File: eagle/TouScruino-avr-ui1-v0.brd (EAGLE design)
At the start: 53.3 x 59.7 mm, 48 parts, among them J1 AVR_ISP, Q1 8MHz, Q2 MMBT2222, Q3 8MHz, U1 ATMEGA1284P, U3 ARDUINO_SHIELD, U4 MCP73831, U5 MIC5209-3.3YS, X1 USB

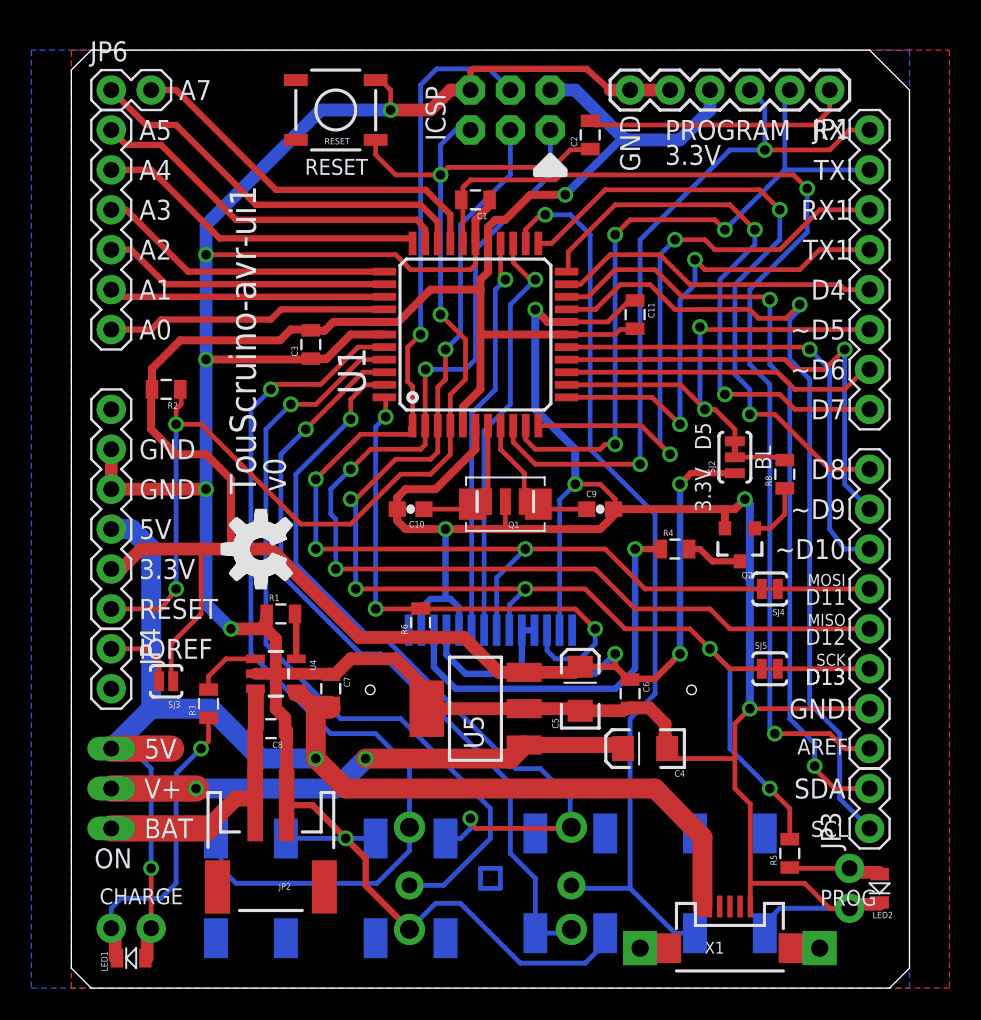
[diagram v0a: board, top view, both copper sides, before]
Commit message: 
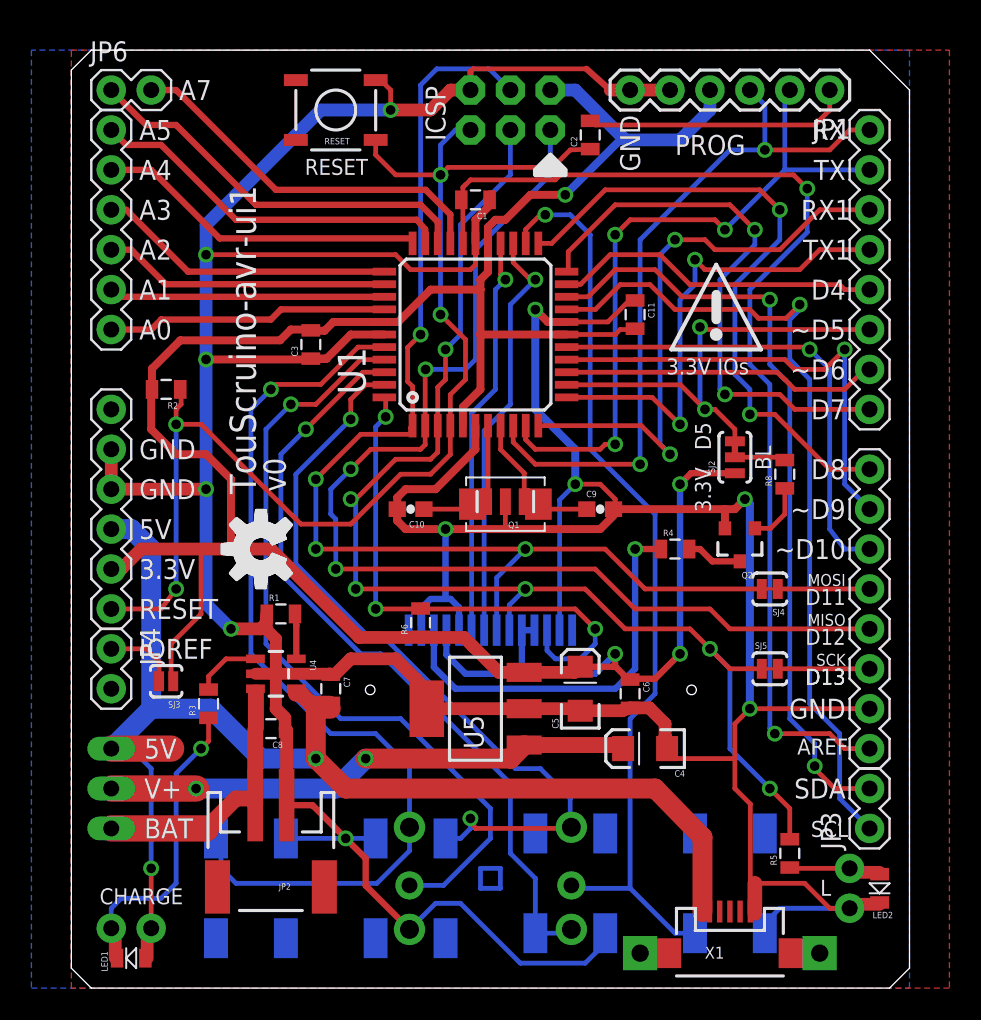
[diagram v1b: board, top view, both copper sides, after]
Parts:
- added U$6: 3.3V_IO, wibauxl:3.3V_IO
- JP1: value M06 -> M06TH
- moved X1 0.32 mm to (41.9, 2.22)
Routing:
- net GND: track 330.0 -> 330.7 mm
- net VUSB: track 84.6 -> 85.3 mm
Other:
- board text added: "L"
- board text removed: "ON"
- board text removed: "PROGRAM 3.3V"
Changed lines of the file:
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@@
 <setting verticaltext="up"/>
 </settings>
-<grid distance="12.5" unitdist="mil" unit="mm" style="lines" multiple="8" display="yes" altdistance="3.125" altunitdist="mil" altunit="mil"/>
+<grid distance="12.5" unitdist="mil" unit="mil" style="lines" multiple="8" display="yes" altdistance="3.125" altunitdist="mil" altunit="mil"/>
 <layers>
 <layer number="1" name="Top" color="4" fill="1" visible="yes" active="yes"/>
@@
 <layer number="27" name="tValues" color="7" fill="1" visible="no" active="yes"/>
 <layer number="28" name="bValues" color="7" fill="1" visible="no" active="yes"/>
-<layer number="29" name="tStop" color="7" fill="3" visible="no" active="yes"/>
+<layer number="29" name="tStop" color="7" fill="3" visible="yes" active="yes"/>
 <layer number="30" name="bStop" color="7" fill="6" visible="no" active="yes"/>
 <layer number="31" name="tCream" color="7" fill="4" visible="no" active="yes"/>
@@
 <layer number="220" name="220bmp" color="21" fill="1" visible="no" active="no"/>
 <layer number="221" name="221bmp" color="22" fill="1" visible="no" active="no"/>
+<layer number="222" name="222bmp" color="23" fill="1" visible="no" active="no"/>
 <layer number="223" name="223bmp" color="24" fill="1" visible="no" active="no"/>
 <layer number="224" name="224bmp" color="25" fill="1" visible="no" active="no"/>
@@
 <text x="44.529375" y="32.972375" size="1.016" layer="21" font="vector" ratio="15" distance="30" rot="R90">BL</text>
 <text x="39.6875" y="33.147" size="1.016" layer="21" font="vector" ratio="15" distance="30" rot="R270">3.3V</text>
-<text x="37.7825" y="52.3875" size="1.27" layer="21" font="vector" ratio="15" distance="25">PROGRAM
-3.3V</text>
+<text x="38.4175" y="53.0225" size="1.27" layer="21" font="vector" ratio="15" distance="25">PROG</text>
 <polygon width="0.3048" layer="21">
 <vertex x="30.48" y="53.0225"/>
@@
 <vertex x="31.4325" y="52.07"/>
 </polygon>
-<text x="1.4605" y="7.62" size="1.27" layer="21" font="vector" ratio="15">ON</text>
-<text x="47.6568" y="5.2387" size="1.016" layer="21" font="vector" ratio="15">PROG</text>
+<text x="47.6568" y="5.8737" size="1.016" layer="21" font="vector" ratio="15">L</text>
 </plain>
 <attributes>
@@
 <element name="JP2" library="SparkFun" package="JST-2-SMD" value="BAT" x="12.7" y="7.9375" rot="R180"/>
 <element name="C8" library="SparkFun" package="0805" value="4.7uF" x="12.7" y="16.51" rot="R180"/>
-<element name="X1" library="wibauxl" package="USB-MICROB" value="USB" x="41.91" y="2.54"/>
+<element name="X1" library="wibauxl" package="USB-MICROB" value="USB" x="41.91" y="2.2225"/>
 <element name="U$3" library="SparkFun" package="OSHW-LOGO-M" value="OSHW-LOGOM" x="12.065" y="27.94" rot="R90"/>
 <element name="JP5" library="wibauxl" package="1X3_LONGPAD" value="SWITCH" x="2.54" y="10.16" rot="MR270"/>
-<element name="JP1" library="wibauxl" package="1X06" value="M06" x="48.26" y="57.15" rot="R180"/>
+<element name="JP1" library="wibauxl" package="1X06" value="M06TH" x="48.26" y="57.15" rot="R180"/>
 <element name="J1" library="SparkFun" package="2X3" value="AVR_ISP" x="30.48" y="54.61" rot="MR0"/>
 <element name="JP3" library="wibauxl" package="1X02" value="I2C" x="50.8" y="10.16" rot="R90"/>
@@
 <element name="SJ4" library="SparkFun" package="SJ_2S-TRACE" value="" x="44.45" y="25.4" rot="R180"/>
 <element name="SJ5" library="SparkFun" package="SJ_2S-TRACE" value="" x="44.45" y="20.32"/>
+<element name="U$6" library="wibauxl" package="3.3V_IO" value="3.3V_IO" x="41.036875" y="42.2275"/>
 </elements>
 <signals>
@@
 <wire x1="35.56" y1="57.15" x2="34.29" y2="57.15" width="0.8128" layer="1"/>
 <wire x1="34.29" y1="57.15" x2="32.781875" y2="58.499375" width="0.4064" layer="1"/>
-<wire x1="32.781875" y1="58.499375" x2="25.55875" y2="58.499375" width="0.4064" layer="1"/>
-<wire x1="25.55875" y1="58.499375" x2="25.4" y2="58.340625" width="0.4064" layer="1"/>
+<wire x1="32.781875" y1="58.499375" x2="25.55875" y2="58.499375" width="0.3048" layer="1"/>
+<wire x1="25.55875" y1="58.499375" x2="25.4" y2="58.340625" width="0.3048" layer="1"/>
 <wire x1="25.4" y1="58.340625" x2="25.4" y2="57.4675" width="0.4064" layer="1"/>
 <wire x1="25.4" y1="57.4675" x2="25.4" y2="57.15" width="0.8128" layer="1"/>
@@
 <wire x1="42.2275" y1="16.8275" x2="42.2275" y2="14.605" width="0.3048" layer="1"/>
 <wire x1="42.2275" y1="16.8275" x2="43.18" y2="17.78" width="0.3048" layer="1"/>
-<wire x1="43.21" y1="5.19" x2="43.21" y2="6.6675" width="0.3048" layer="1"/>
+<wire x1="43.21" y1="4.8725" x2="43.4975" y2="4.7625" width="0.3048" layer="1"/>
+<wire x1="43.4975" y1="4.7625" x2="43.4975" y2="6.6675" width="0.9398" layer="1"/>
+<wire x1="43.4975" y1="6.6675" x2="43.21" y2="6.6675" width="0.3048" layer="1"/>
 <wire x1="43.21" y1="6.6675" x2="43.21" y2="11.7175" width="0.3048" layer="1"/>
 <wire x1="43.21" y1="11.7175" x2="42.2275" y2="12.7" width="0.3048" layer="1"/>
@@
 <wire x1="49.53" y1="5.08" x2="48.26" y2="5.08" width="0.3048" layer="1"/>
 <wire x1="48.26" y1="5.08" x2="46.6725" y2="6.6675" width="0.3048" layer="1"/>
-<wire x1="46.6725" y1="6.6675" x2="43.21" y2="6.6675" width="0.3048" layer="1"/>
+<wire x1="46.6725" y1="6.6675" x2="43.4975" y2="6.6675" width="0.3048" layer="1"/>
 <wire x1="44.1325" y1="4.1275" x2="45.085" y2="5.08" width="0.3048" layer="16"/>
 <wire x1="45.085" y1="5.08" x2="49.53" y2="5.08" width="0.3048" layer="16"/>
@@
 <wire x1="2.54" y1="15.24" x2="6.35" y2="15.24" width="1.6764" layer="1"/>
 <wire x1="5.08" y1="17.78" x2="2.54" y2="15.24" width="1.27" layer="16"/>
-<wire x1="40.3225" y1="5.19" x2="40.16375" y2="5.159375" width="0.4064" layer="1"/>
-<wire x1="40.16375" y1="5.159375" x2="40.16375" y2="9.604375" width="1.27" layer="1"/>
+<wire x1="40.3225" y1="5.19" x2="40.16375" y2="4.841875" width="0.4064" layer="1"/>
+<wire x1="40.16375" y1="4.841875" x2="40.16375" y2="9.604375" width="1.27" layer="1"/>
 <wire x1="40.16375" y1="9.604375" x2="37.1475" y2="12.7" width="1.27" layer="1"/>
-<wire x1="40.3225" y1="5.19" x2="40.61" y2="5.19" width="0.127" layer="1"/>
+<wire x1="40.3225" y1="5.19" x2="40.61" y2="4.8725" width="0.127" layer="1"/>
 </signal>
 <signal name="N$13">
@@
 </board>
 </drawing>
-<compatibility>
-<note version="6.3" minversion="6.2.2" severity="warning">
-Since Version 6.2.2 text objects can contain more than one line,
-which will not be processed correctly with this version.
-</note>
-</compatibility>
 </eagle>

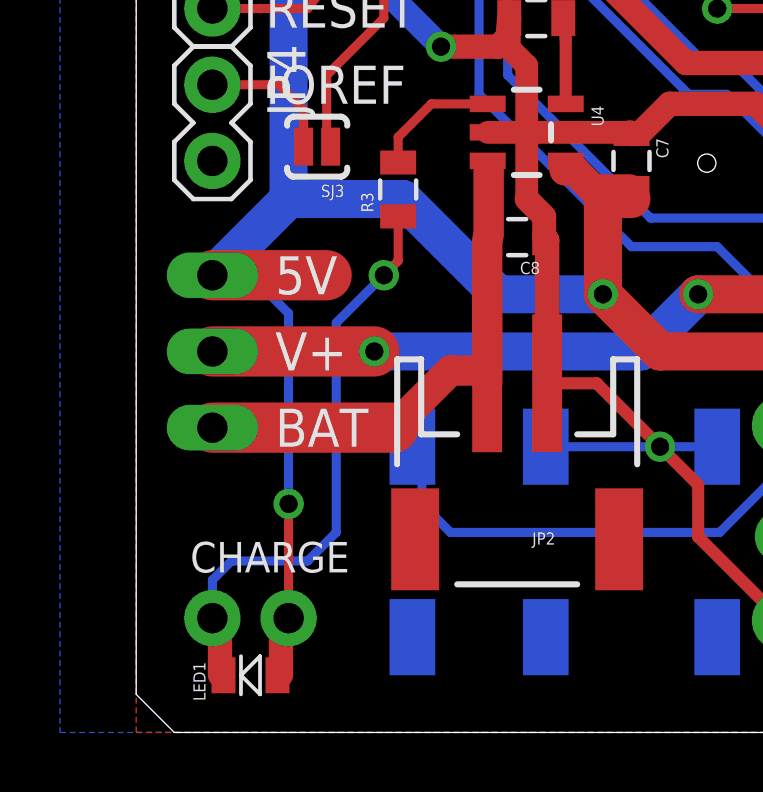
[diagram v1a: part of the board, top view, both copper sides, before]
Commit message: 
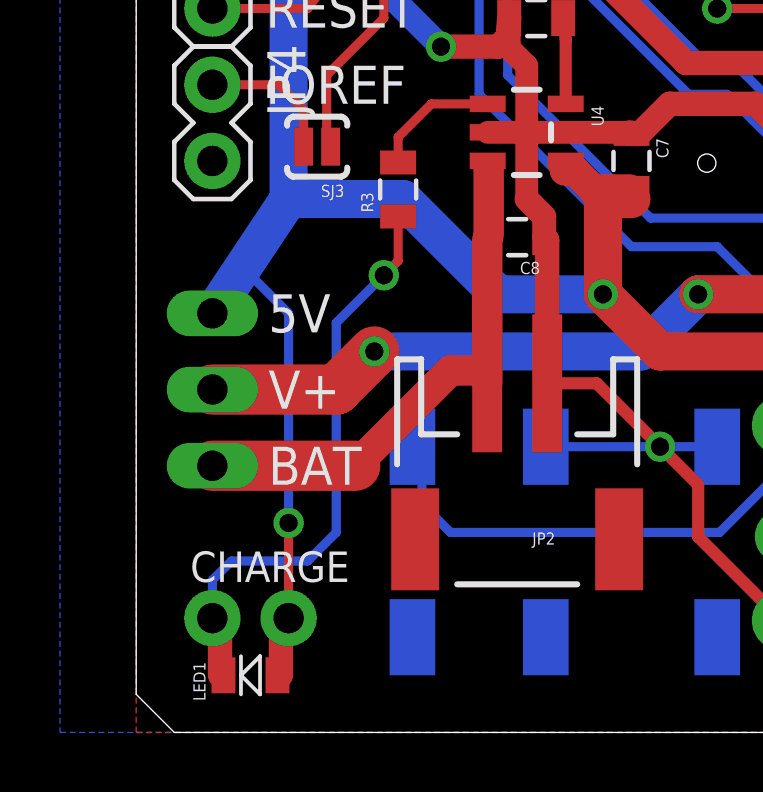
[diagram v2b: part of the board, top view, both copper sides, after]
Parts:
- moved JP5 1.27 mm to (2.54, 8.89)
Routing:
- net VUSB: track 85.3 -> 83.0 mm
- net VBAT: track 18.1 -> 18.6 mm
- net V+: track 34.1 -> 34.6 mm
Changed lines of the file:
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@@
 <layer number="22" name="bPlace" color="7" fill="1" visible="no" active="yes"/>
 <layer number="23" name="tOrigins" color="15" fill="1" visible="yes" active="yes"/>
-<layer number="24" name="bOrigins" color="15" fill="1" visible="no" active="yes"/>
+<layer number="24" name="bOrigins" color="15" fill="1" visible="yes" active="yes"/>
 <layer number="25" name="tNames" color="7" fill="1" visible="no" active="yes"/>
 <layer number="26" name="bNames" color="7" fill="1" visible="no" active="yes"/>
@@
 <text x="4.318" y="26.035" size="1.27" layer="21" font="vector" ratio="15">3.3V</text>
 <text x="4.318" y="23.495" size="1.27" layer="21" font="vector" ratio="15">RESET</text>
-<text x="4.6355" y="9.525" size="1.27" layer="21" font="vector" ratio="15">BAT</text>
-<text x="4.6355" y="12.065" size="1.27" layer="21" font="vector" ratio="15">V+</text>
-<text x="7.112" y="6.35" size="1.016" layer="21" font="vector" ratio="15" rot="R180">CHARGE</text>
+<text x="4.4069" y="8.255" size="1.27" layer="21" font="vector" ratio="15">BAT</text>
+<text x="4.4069" y="10.795" size="1.27" layer="21" font="vector" ratio="15">V+</text>
+<text x="7.112" y="6.0325" size="1.016" layer="21" font="vector" ratio="15" rot="R180">CHARGE</text>
 <text x="39.6875" y="36.0045" size="1.016" layer="21" font="vector" ratio="15" distance="30" rot="R270">D5</text>
 <text x="49.276" y="18.415" size="1.27" layer="21" font="vector" ratio="15" rot="R180">GND</text>
@@
 <text x="49.43475" y="15.875" size="1.016" layer="21" font="vector" ratio="15" rot="R180">AREF</text>
 <text x="6.858" y="56.515" size="1.27" layer="21" font="vector" ratio="15">A7</text>
-<text x="4.6355" y="14.605" size="1.27" layer="21" font="vector" ratio="15">5V</text>
+<text x="4.4069" y="13.335" size="1.27" layer="21" font="vector" ratio="15">5V</text>
 <text x="44.529375" y="32.972375" size="1.016" layer="21" font="vector" ratio="15" distance="30" rot="R90">BL</text>
 <text x="39.6875" y="33.147" size="1.016" layer="21" font="vector" ratio="15" distance="30" rot="R270">3.3V</text>
@@
 <element name="X1" library="wibauxl" package="USB-MICROB" value="USB" x="41.91" y="2.2225"/>
 <element name="U$3" library="SparkFun" package="OSHW-LOGO-M" value="OSHW-LOGOM" x="12.065" y="27.94" rot="R90"/>
-<element name="JP5" library="wibauxl" package="1X3_LONGPAD" value="SWITCH" x="2.54" y="10.16" rot="MR270"/>
+<element name="JP5" library="wibauxl" package="1X3_LONGPAD" value="SWITCH" x="2.54" y="8.89" rot="MR270"/>
 <element name="JP1" library="wibauxl" package="1X06" value="M06TH" x="48.26" y="57.15" rot="R180"/>
 <element name="J1" library="SparkFun" package="2X3" value="AVR_ISP" x="30.48" y="54.61" rot="MR0"/>
@@
 <wire x1="12.065" y1="14.605" x2="15.5575" y2="14.605" width="1.27" layer="16"/>
 <via x="15.5575" y="14.605" extent="1-16" drill="0.6096"/>
-<wire x1="5.08" y1="3.81" x2="5.08" y2="7.62" width="0.3048" layer="1"/>
-<wire x1="5.08" y1="7.62" x2="5.08" y2="13.97" width="0.3048" layer="16"/>
+<wire x1="5.08" y1="3.81" x2="5.08" y2="6.985" width="0.3048" layer="1"/>
+<wire x1="5.08" y1="6.985" x2="5.08" y2="13.97" width="0.3048" layer="16"/>
 <wire x1="5.08" y1="13.97" x2="3.81" y2="15.24" width="0.3048" layer="16"/>
-<wire x1="3.81" y1="15.24" x2="2.54" y2="15.24" width="0.3048" layer="16"/>
-<via x="5.08" y="7.62" extent="1-16" drill="0.6096"/>
+<wire x1="3.81" y1="15.24" x2="2.54" y2="13.97" width="0.3048" layer="16"/>
+<via x="5.08" y="6.985" extent="1-16" drill="0.6096"/>
 <wire x1="2.54" y1="29.21" x2="3.81" y2="29.21" width="1.27" layer="16"/>
 <wire x1="3.81" y1="29.21" x2="5.08" y2="27.94" width="1.27" layer="16"/>
@@
 <wire x1="16.51" y1="17.78" x2="15.5575" y2="17.78" width="1.27" layer="1"/>
 <wire x1="15.5575" y1="17.78" x2="15.5575" y2="14.605" width="1.27" layer="1"/>
-<wire x1="2.54" y1="15.24" x2="6.35" y2="15.24" width="1.6764" layer="1"/>
-<wire x1="5.08" y1="17.78" x2="2.54" y2="15.24" width="1.27" layer="16"/>
+<wire x1="5.08" y1="17.78" x2="2.54" y2="13.97" width="1.27" layer="16"/>
 <wire x1="40.3225" y1="5.19" x2="40.16375" y2="4.841875" width="0.4064" layer="1"/>
 <wire x1="40.16375" y1="4.841875" x2="40.16375" y2="9.604375" width="1.27" layer="1"/>
@@
 <wire x1="11.7" y1="11.6375" x2="11.7" y2="16.41" width="1.016" layer="1"/>
 <wire x1="11.7" y1="16.41" x2="11.8" y2="16.51" width="0.8128" layer="1"/>
-<wire x1="2.54" y1="10.16" x2="8.5725" y2="10.16" width="1.6764" layer="1"/>
-<wire x1="8.5725" y1="10.16" x2="10.4775" y2="12.065" width="1.016" layer="1"/>
+<wire x1="2.54" y1="8.89" x2="7.3025" y2="8.89" width="1.6764" layer="1"/>
+<wire x1="7.3025" y1="8.89" x2="10.4775" y2="12.065" width="1.016" layer="1"/>
 <wire x1="10.4775" y1="12.065" x2="11.2725" y2="12.065" width="1.016" layer="1"/>
 <wire x1="11.2725" y1="12.065" x2="11.7" y2="11.6375" width="0.8128" layer="1"/>
@@
 <contactref element="C4" pad="A"/>
 <contactref element="JP5" pad="2"/>
-<wire x1="2.54" y1="12.7" x2="7.9375" y2="12.7" width="1.6764" layer="1"/>
+<wire x1="2.54" y1="11.43" x2="6.6675" y2="11.43" width="1.6764" layer="1"/>
+<wire x1="6.6675" y1="11.43" x2="7.9375" y2="12.7" width="1.6764" layer="1"/>
 <wire x1="27.9527" y1="14.605" x2="28.8163" y2="15.4686" width="1.27" layer="1"/>
 <via x="7.9375" y="12.7" extent="1-16" drill="0.6096"/>
